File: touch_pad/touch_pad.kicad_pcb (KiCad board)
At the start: 2 copper layers, 70 x 14 mm, 18 parts, among them J1 I/O connector, U1 HT7550-1, U2 TLV6001UIDBVR

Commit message: Complete
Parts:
- J1: footprint cycfi_library:pin_header_1x3p_2.54mm_smd_horizontal -> Connector_PinHeader_2.54mm:PinHeader_1x03_P2.54mm_Vertical_SMD_Pin1Left
- moved R6 43.3 mm to (151.0, 101.0), turned to 180 degrees
- moved R4 41.3 mm to (151.0, 103.0)
- moved R9 38.4 mm to (162.3, 107.3), turned to 180 degrees
- moved R3 29.7 mm to (170.0, 105.0), turned to 180 degrees
- moved R5 28.7 mm to (170.0, 106.5), turned to 180 degrees
- moved R7 25.9 mm to (179.5, 103.8)
- moved R8 21.8 mm to (176.5, 100.8), turned to -90 degrees
- moved U2 21.4 mm to (179.5, 100.8)
- moved C1 20.9 mm to (165.2, 100.5)
- moved C2 20.9 mm to (165.2, 102.8)
- moved C3 20.7 mm to (173.8, 97.8), turned to 90 degrees
- moved U1 20.3 mm to (170.4, 98.6)
- moved D1 20.2 mm to (165.2, 97.2)
- moved J1 19.3 mm to (159.0, 102.0)
- moved RV1 15.5 mm to (174.4, 105.0)
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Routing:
- net Net-(C3-Pad1): track 0.00 -> 54.4 mm, vias 0 -> 3
- net 5v: track 0.00 -> 32.5 mm
- net Net-(R9-Pad1): track 0.00 -> 22.2 mm
- net Net-(R7-Pad1): track 0.00 -> 9.82 mm
- net GND: track 0.00 -> 7.32 mm, vias 0 -> 8
- net Net-(C1-Pad1): track 0.00 -> 5.37 mm
- net Net-(R2-Pad2): track 0.00 -> 4.49 mm, vias 0 -> 1
- net V+: track 0.00 -> 3.83 mm
- net OUT: track 0.00 -> 3.23 mm
- net Net-(R1-Pad1): track 0.00 -> 3.05 mm, vias 0 -> 1
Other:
- board text added: "SENS"

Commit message: Minor tweaks
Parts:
- removed the G*** at (138.0, 97.0)
- added G***: LOGO, cycfi_library:cycfi-logo-12mm, F.Cu at (145.4, 96.7)
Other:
- board text added: "Touch Pad v0.9"

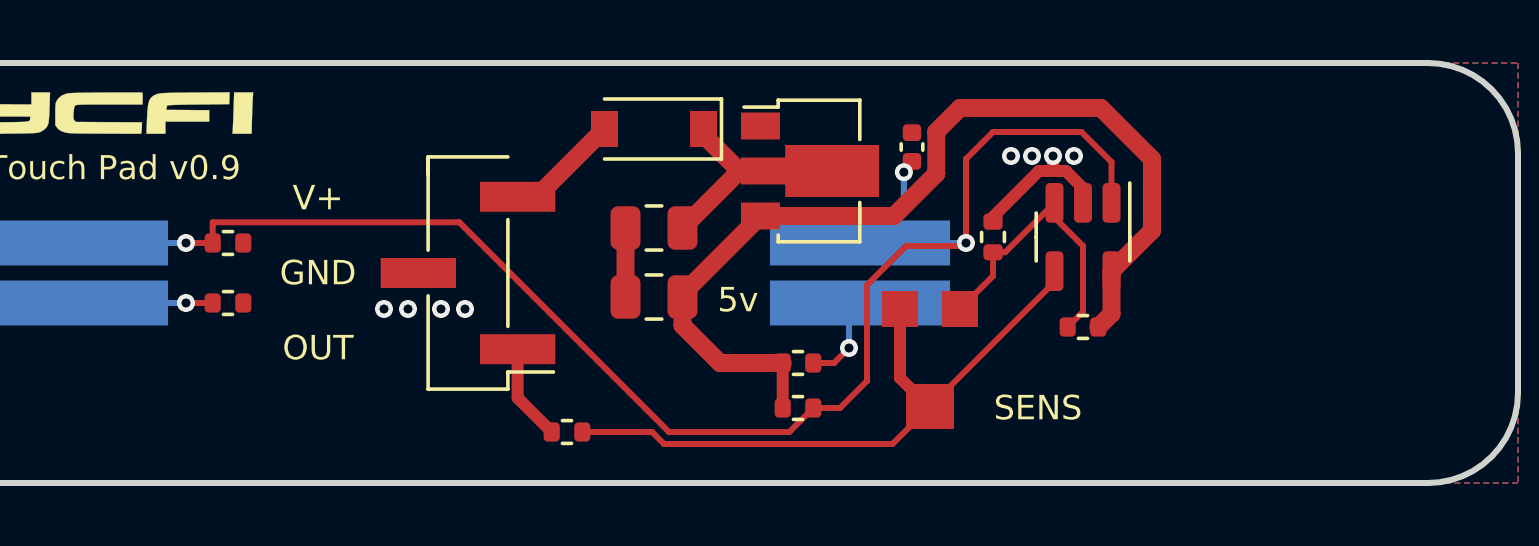
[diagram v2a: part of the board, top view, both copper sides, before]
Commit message: Place components away from board edge
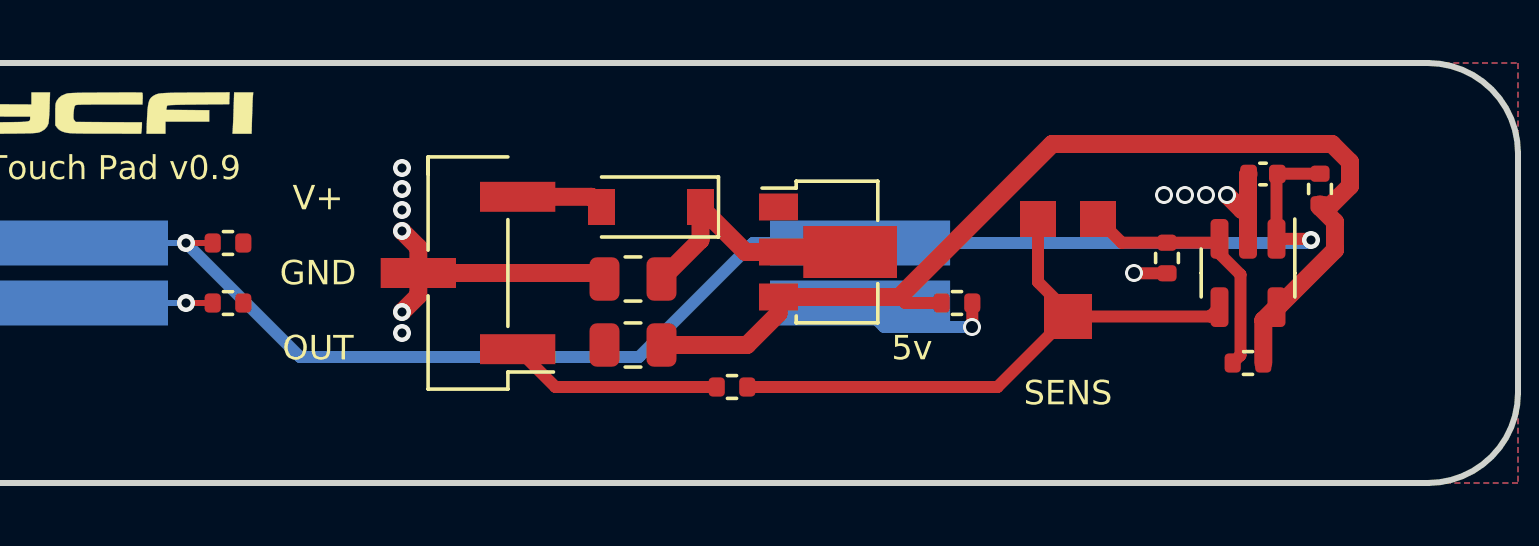
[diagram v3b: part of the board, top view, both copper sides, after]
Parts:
- moved R5 18.9 mm to (187.4, 99.2), turned to -90 degrees
- moved C3 11.7 mm to (185.5, 98.7), turned to 180 degrees
- moved R8 5.84 mm to (182.3, 101.5), turned to 90 degrees
- moved R9 5.70 mm to (167.8, 105.8)
- moved R3 5.66 mm to (175.3, 103.0)
- moved R7 5.63 mm to (185.0, 105.0)
- moved U2 5.63 mm to (185.0, 102.0)
- moved RV1 5.49 mm to (179.0, 102.0)
- moved U1 2.77 mm to (171.0, 101.3)
- moved D1 2.60 mm to (165.1, 99.8)
- moved C1 1.84 mm to (164.5, 102.2)
- moved C2 1.75 mm to (164.5, 104.4)
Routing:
- net GND: track 7.32 -> 13.6 mm, vias 8 -> 11
- net Net-(C3-Pad1): track 54.4 -> 49.9 mm, vias 3 -> 2
- net OUT: track 3.23 -> 7.16 mm
- net 5v: track 32.5 -> 36.4 mm
- net Net-(R1-Pad1): track 3.05 -> 4.87 mm
- net Net-(R9-Pad1): track 22.2 -> 20.5 mm
- net V+: track 3.83 -> 2.94 mm
- net Net-(C1-Pad1): track 5.37 -> 6.25 mm
- net Net-(R7-Pad1): track 9.82 -> 8.97 mm
